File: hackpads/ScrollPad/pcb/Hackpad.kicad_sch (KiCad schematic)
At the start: 10 parts, among them SW1 SW_Push, SW2 SW_Push, SW3 SW_Push, SW4 SW_Push, SW5 SW_Push, U1 XIAO-RP2040-DIP

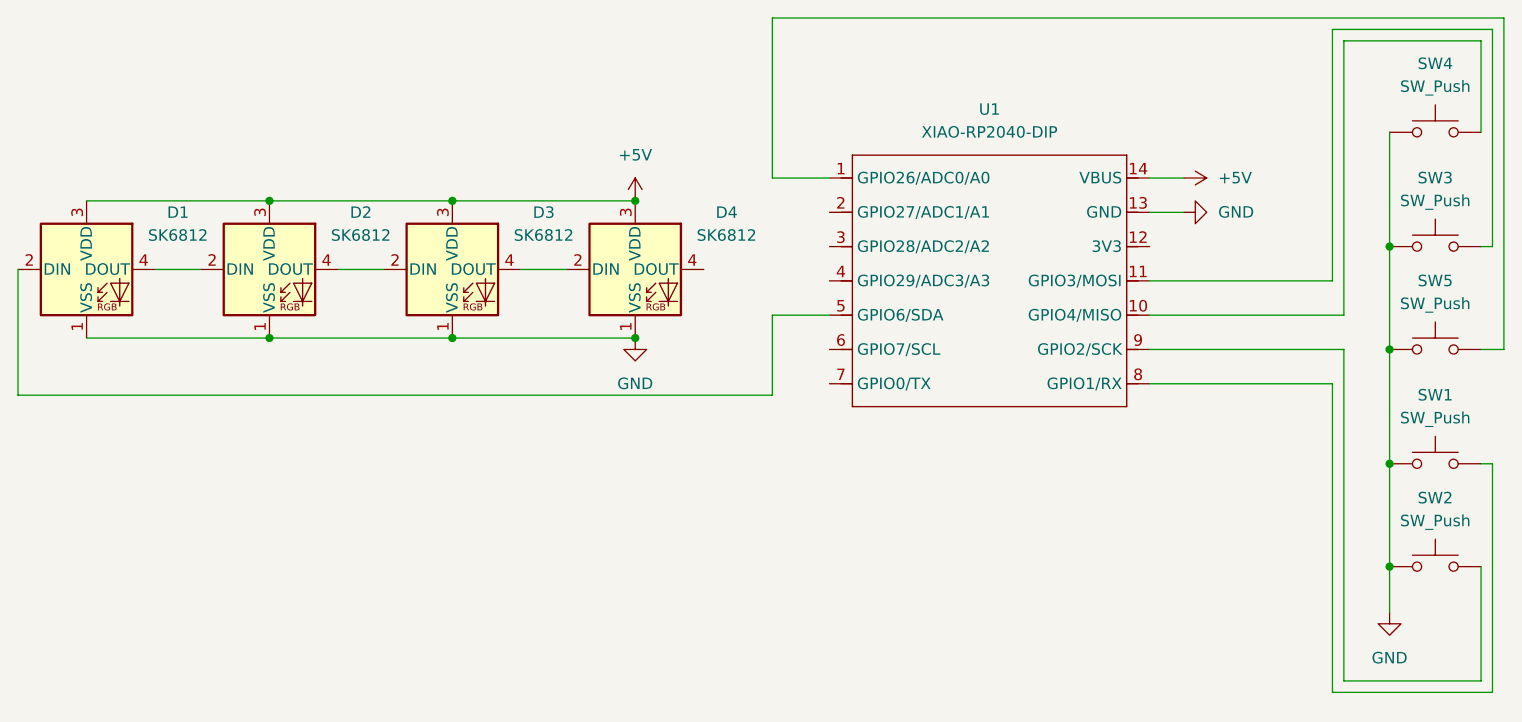
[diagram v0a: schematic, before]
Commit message: Update ScrollPad hardware and firmware
- Change GPIO pin assignments
- PCB improvements: add mounting holes, LED position, routing
- Case improvements: add spacer, cover fix, add Skadis holder
- Update firmware: add LED layer indication, add mouse scrolling keys, change keys
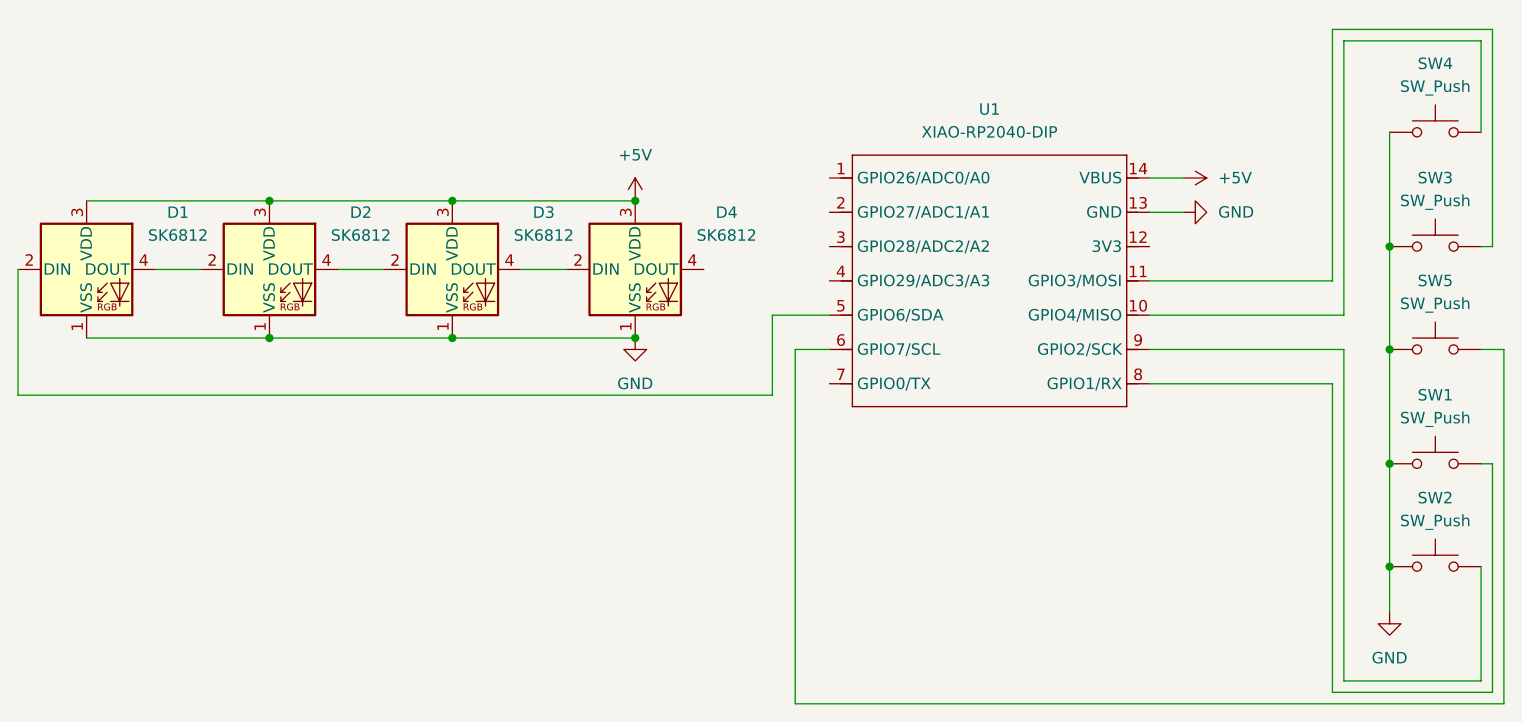
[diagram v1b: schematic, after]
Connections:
- net at U1.1 (GPIO26/ADC0/A0): no longer SW5.2
- net at U1.6 (GPIO7/SCL): now also SW5.2
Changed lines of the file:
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@@
+	(wire
+		(pts
+			(xy 223.52 62.23) (xy 226.06 62.23)
+		)
+		(stroke
+			(width 0)
+			(type default)
+		)
+	)
 	(wire
 		(pts
@@
 	(wire
 		(pts
+			(xy 147.32 101.6) (xy 147.32 62.23)
+		)
+		(stroke
+			(width 0)
+			(type default)
+		)
+	)
+	(wire
+		(pts
 			(xy 207.01 54.61) (xy 186.69 54.61)
 		)
@@
 	(wire
 		(pts
+			(xy 226.06 101.6) (xy 147.32 101.6)
+		)
+		(stroke
+			(width 0)
+			(type default)
+		)
+	)
+	(wire
+		(pts
 			(xy 109.22 60.96) (xy 129.54 60.96)
 		)
@@
 	(wire
 		(pts
-			(xy 144.78 25.4) (xy 144.78 43.18)
-		)
-		(stroke
-			(width 0)
-			(type default)
-		)
-	)
-	(wire
-		(pts
 			(xy 116.84 53.34) (xy 121.92 53.34)
 		)
@@
 	(wire
 		(pts
+			(xy 226.06 62.23) (xy 226.06 101.6)
+		)
+		(stroke
+			(width 0)
+			(type default)
+		)
+	)
+	(wire
+		(pts
 			(xy 223.52 86.36) (xy 223.52 99.06)
 		)
@@
 	(wire
 		(pts
+			(xy 147.32 62.23) (xy 151.13 62.23)
+		)
+		(stroke
+			(width 0)
+			(type default)
+		)
+	)
+	(wire
+		(pts
 			(xy 208.28 99.06) (xy 208.28 62.23)
 		)
@@
 	(wire
 		(pts
-			(xy 226.06 25.4) (xy 144.78 25.4)
-		)
-		(stroke
-			(width 0)
-			(type default)
-		)
-	)
-	(wire
-		(pts
 			(xy 88.9 60.96) (xy 109.22 60.96)
 		)
@@
 	(wire
 		(pts
-			(xy 223.52 62.23) (xy 226.06 62.23)
-		)
-		(stroke
-			(width 0)
-			(type default)
-		)
-	)
-	(wire
-		(pts
 			(xy 186.69 46.99) (xy 190.5 46.99)
 		)
@@
 	(wire
 		(pts
-			(xy 226.06 62.23) (xy 226.06 25.4)
-		)
-		(stroke
-			(width 0)
-			(type default)
-		)
-	)
-	(wire
-		(pts
 			(xy 213.36 38.1) (xy 213.36 50.8)
 		)
 		(stroke
-			(width 0)
-			(type default)
-		)
-	)
-	(wire
-		(pts
-			(xy 144.78 43.18) (xy 151.13 43.18)
-		)
-		(stroke
